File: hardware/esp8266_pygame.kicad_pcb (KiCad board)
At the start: 2 copper layers, 73 parts, among them J1 Conn_02x02_Odd_Even, J2 Conn_01x02, J3 USB_C_Receptacle_USB2.0_16P, J4 Conn_01x07, J5 Conn_01x07, J6 Conn_01x08, Q1 PNP, Q2 NPN, SW1 SW_Push, SW2 SW_Push, SW3 SW_Push, SW4 SW_Push, SW5 SW_Push, SW6 SW_Push, SW7 SW_Push, SW8 SW_Push, U1 ESP-07, U2 SW_SPDT_3pin, U3 HX3242, U4 TP4056, U5 FS8502A, U6 DW01A, U7 AP2112K-3.3, U8 PCF8574T

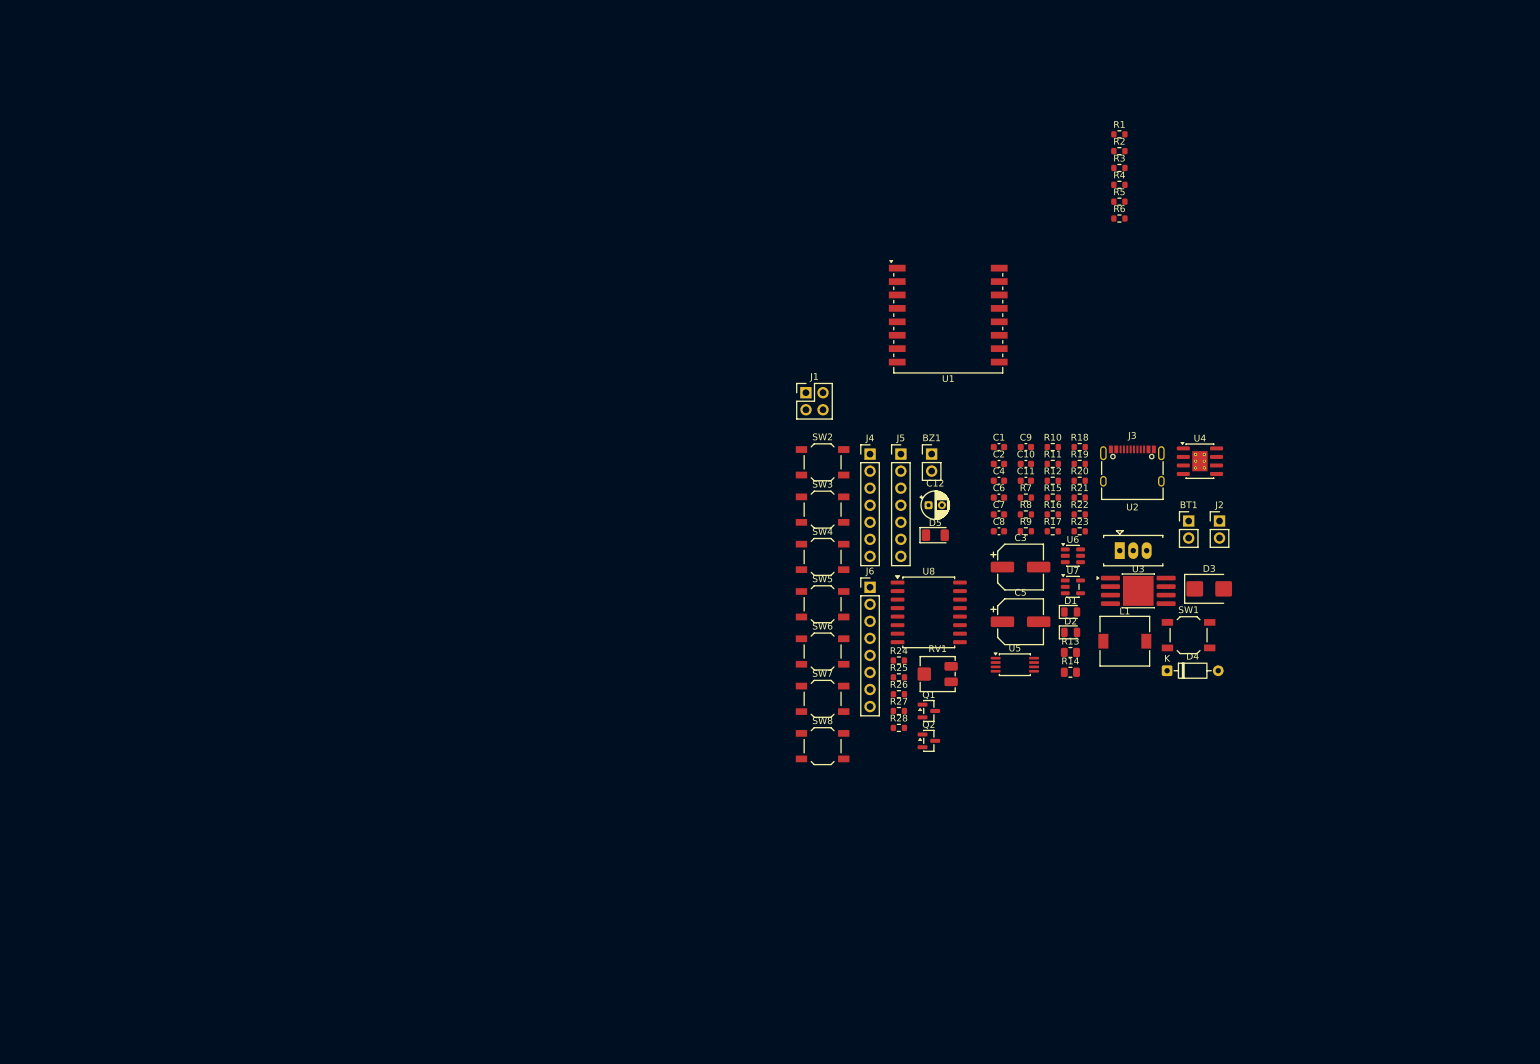
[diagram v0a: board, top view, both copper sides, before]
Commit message: Initial PCB placement and some schematic changes
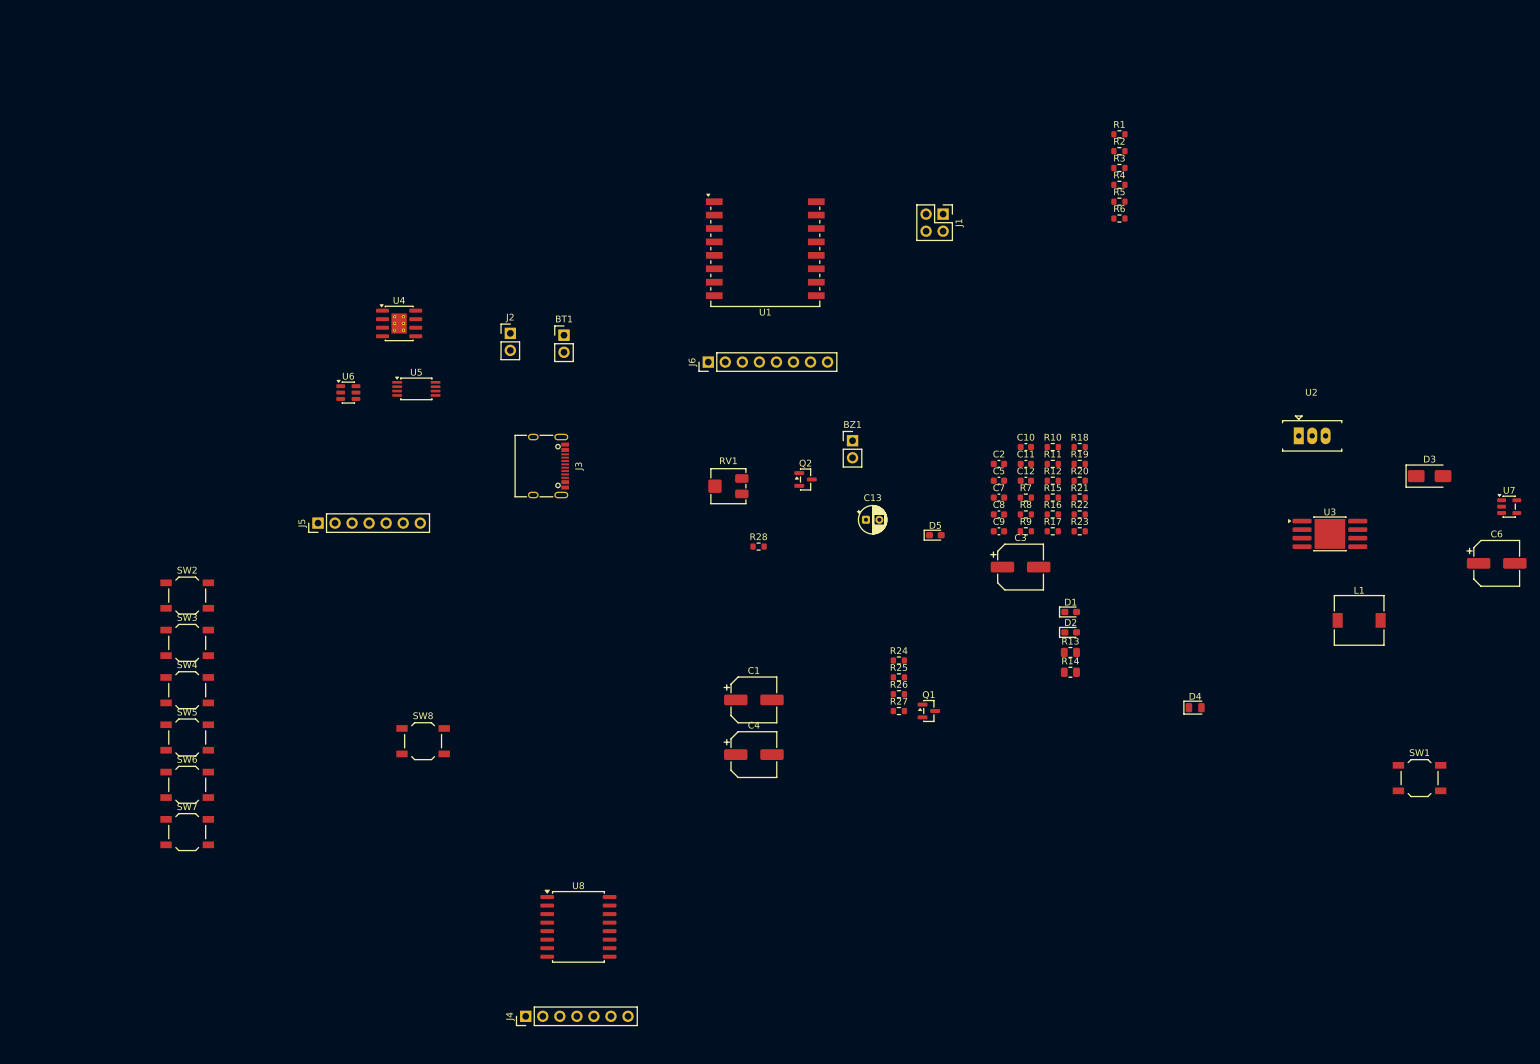
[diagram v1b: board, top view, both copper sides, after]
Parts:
- added C4: 1u, Capacitor_SMD:CP_Elec_6.3x3, F.Cu at (122.8, 148.0)
- C1: value 100n -> 100u; footprint Capacitor_SMD:C_0603_1608Metric -> Capacitor_SMD:CP_Elec_6.3x3
- D1, D2: footprint Diode_SMD:D_0805_2012Metric -> Diode_SMD:D_0603_1608Metric_Pad1.05x0.95mm_HandSolder
- D3: footprint Diode_SMD:D_SMB -> Diode_SMD:D_SMA
- D4: value 1N4148 -> D; footprint Diode_THT:D_DO-35_SOD27_P7.62mm_Horizontal -> Diode_SMD:D_0805_2012Metric
- D5: footprint LED_SMD:LED_1206_3216Metric -> Diode_SMD:D_0603_1608Metric_Pad1.05x0.95mm_HandSolder
- moved U4 121.1 mm to (69.9, 83.8)
- moved U6 110.7 mm to (62.4, 94.0)
- moved J2 109.3 mm to (86.5, 85.2)
- moved J4 98.2 mm to (88.8, 187.0), turned to 90 degrees
- moved U5 98.2 mm to (72.5, 93.5)
- moved BT1 97.1 mm to (94.5, 85.5)
- moved SW6 96.8 mm to (38.4, 152.5)
- moved SW7 96.8 mm to (38.4, 159.6)
- moved SW2 96.8 mm to (38.4, 124.3)
- moved SW3 96.8 mm to (38.4, 131.3)
- moved SW4 96.8 mm to (38.4, 138.4)
- moved SW5 96.8 mm to (38.4, 145.4)
- moved J3 88.2 mm to (91.0, 105.0), turned to -90 degrees
- moved J5 87.5 mm to (57.8, 113.5), turned to 90 degrees
- moved C6 71.5 mm to (233.5, 119.5)
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- renumbered C9 to C10, C10 to C11, C11 to C12, C12 to C13, C4 to C5, C5 to C6, C6 to C7, C7 to C8, C8 to C9
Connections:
- C1 pad 1: GND -> +VSW
- C1 pad 2: +VSW -> GND

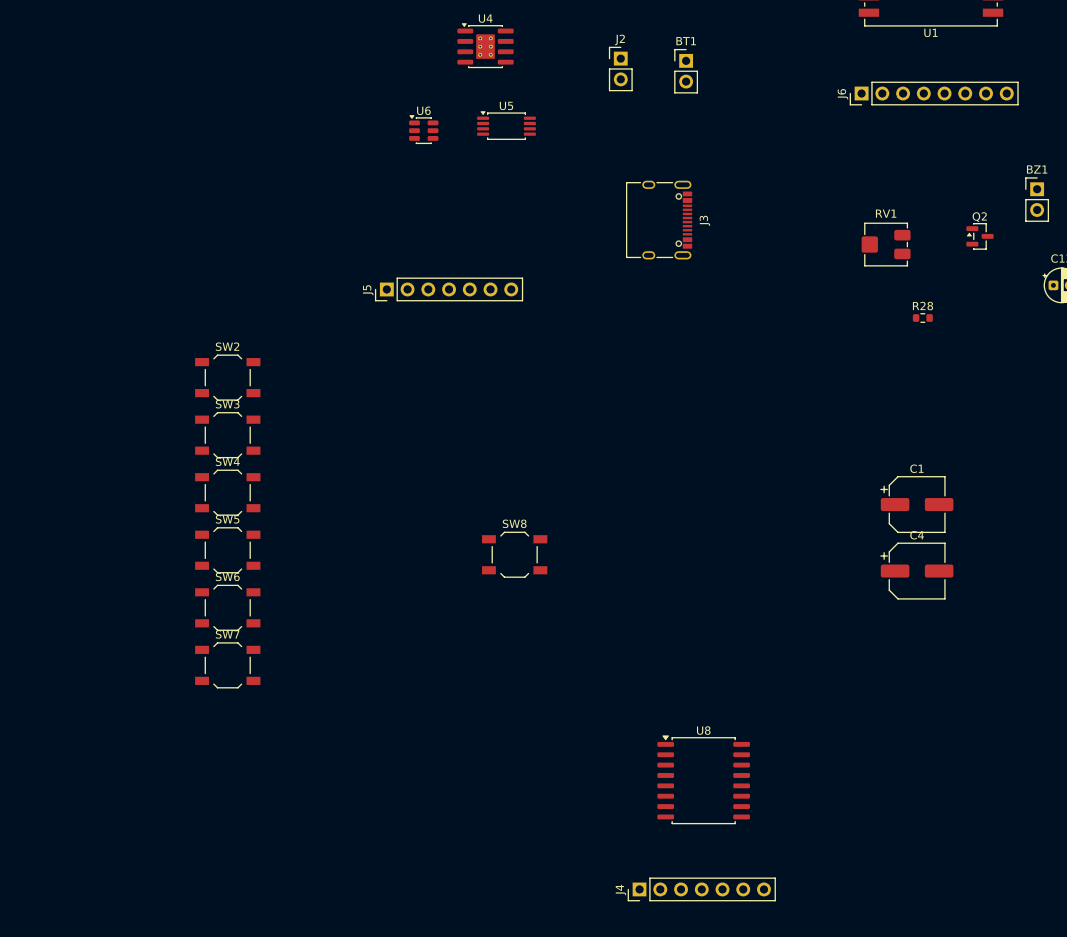
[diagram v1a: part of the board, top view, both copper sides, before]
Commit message: Fixed keypad connector
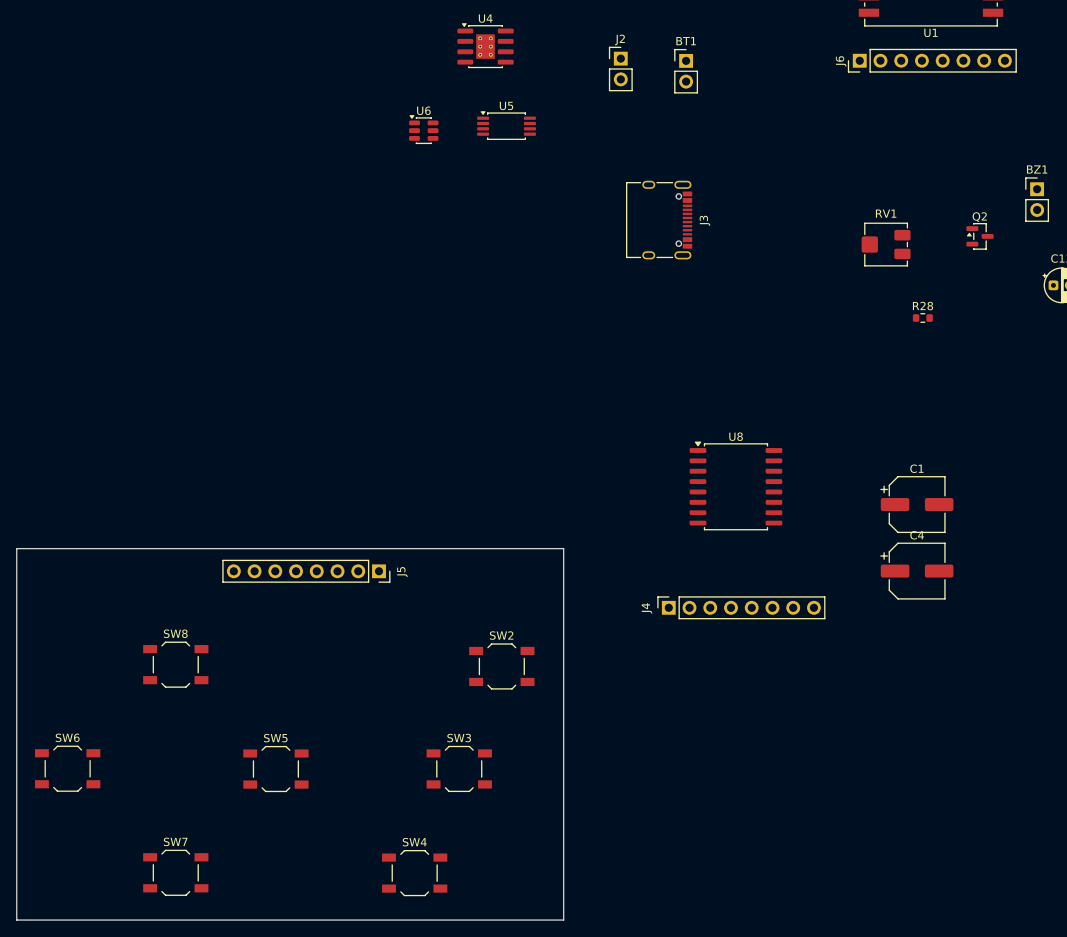
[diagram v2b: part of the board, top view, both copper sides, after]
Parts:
- J4, J5: value Conn_01x07 -> Conn_01x08; footprint Connector_PinHeader_2.54mm:PinHeader_1x07_P2.54mm_Vertical -> Connector_PinSocket_2.54mm:PinSocket_1x08_P2.54mm_Vertical
- moved SW4 51.9 mm to (61.2, 185.0)
- moved SW3 49.8 mm to (66.7, 172.2)
- moved SW2 48.8 mm to (71.9, 159.7)
- moved SW8 43.6 mm to (32.0, 159.5)
- moved U8 36.2 mm to (100.6, 137.7)
- moved J4 34.7 mm to (92.4, 152.5)
- moved J5 34.5 mm to (56.9, 148.0), turned to -90 degrees
- moved SW6 27.8 mm to (18.7, 172.2)
- moved SW5 27.4 mm to (44.2, 172.2)
- moved SW7 26.2 mm to (32.0, 185.0)
- moved J6 4.02 mm to (115.8, 85.5)
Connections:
- SW2 pad 2: GND -> /Human Machine Interface Section/BTN_GND
- SW3 pad 2: GND -> /Human Machine Interface Section/BTN_GND
- SW4 pad 2: GND -> /Human Machine Interface Section/BTN_GND
- SW5 pad 2: GND -> /Human Machine Interface Section/BTN_GND
- SW6 pad 2: GND -> /Human Machine Interface Section/BTN_GND
- SW7 pad 2: GND -> /Human Machine Interface Section/BTN_GND
- SW8 pad 2: GND -> /Human Machine Interface Section/BTN_GND
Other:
- board outline added: 67 x 45.5 mm

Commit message: Audio improvements
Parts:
- removed the C4 at (122.8, 148.0)
- removed Q2: NPN, Package_TO_SOT_SMD:SOT-23
- added C13: 100n, Capacitor_SMD:C_0603_1608Metric, F.Cu at (172.2, 94.6)
- added C14: 10n, Capacitor_SMD:C_0603_1608Metric, F.Cu at (172.2, 97.2)
- added C15: 10u, Capacitor_THT:CP_Radial_D4.0mm_P2.00mm, F.Cu at (176.0, 96.2)
- added C16: 47n, Capacitor_SMD:C_0603_1608Metric, F.Cu at (172.2, 99.7)
- added C17: 220u, Capacitor_THT:CP_Radial_D4.0mm_P2.00mm, F.Cu at (176.0, 101.7)
- added R29: 10k, Resistor_SMD:R_0603_1608Metric, F.Cu at (172.2, 104.7)
- added R30: 10, Resistor_SMD:R_0603_1608Metric, F.Cu at (172.2, 107.2)
- added U9: LM386, Package_SO:SO-8_3.9x4.9mm_P1.27mm, F.Cu at (178.4, 107.8)
- moved R8 137.1 mm to (40.8, 50.7)
- moved R7 135.3 mm to (40.8, 52.5)
- moved D2 131.0 mm to (69.9, 45.2), turned to 90 degrees
- moved C2 129.2 mm to (40.0, 55.2), turned to 90 degrees
- moved D1 127.7 mm to (71.8, 45.2), turned to 90 degrees
- moved R12 117.7 mm to (65.4, 48.2), turned to 180 degrees
- moved R11 115.7 mm to (65.4, 50.0), turned to 180 degrees
- moved R15 108.0 mm to (63.0, 82.0), turned to 90 degrees
- moved R19 105.3 mm to (66.2, 98.5)
- moved R23 102.2 mm to (72.5, 88.8)
- moved C11 101.1 mm to (64.0, 88.2)
- moved J3 79.4 mm to (33.0, 50.7)
- moved C1 77.8 mm to (199.7, 127.8)
- moved R2 69.4 mm to (112.0, 81.8), turned to 90 degrees
- moved R9 69.2 mm to (101.0, 84.8)
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- renumbered C11 to C10, C12 to C11, C13 to C12, C5 to C4, C6 to C5, C7 to C6, C8 to C7, C9 to C8, C10 to C9
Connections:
- BZ1 pad 1: +3.3V -> Net-(BZ1--)
- BZ1 pad 2: Net-(BZ1-+) -> GND
- J4 pad 5: /Human Machine Interface Section/Left_Button_CONN -> GND
- J4 pad 8: GND -> /Human Machine Interface Section/Left_Button_CONN
- J5 pad 5: /Human Machine Interface Section/Left_Button -> /Human Machine Interface Section/BTN_GND
- J5 pad 8: /Human Machine Interface Section/BTN_GND -> /Human Machine Interface Section/Left_Button
- R28 pad 1: Net-(R28-Pad1) -> /BUZZER
- RV1 pad 2: /BUZZER -> Net-(C14-Pad2)
- RV1 pad 3: Net-(R28-Pad1) -> Net-(U9-+)
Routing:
- net /Human Machine Interface Section/Left_Button: track 0.00 -> 39.0 mm
- net /Human Machine Interface Section/Down_Button: track 0.00 -> 38.8 mm
- net /Human Machine Interface Section/C_Button: track 0.00 -> 37.7 mm
- net /Human Machine Interface Section/B_Button: track 0.00 -> 27.0 mm
- net /Human Machine Interface Section/Right_Button: track 0.00 -> 23.1 mm
- net /Human Machine Interface Section/UP_Button_CONN: track 0.00 -> 20.2 mm
- net /Human Machine Interface Section/A_Button_CONN: track 0.00 -> 19.4 mm
- net /Human Machine Interface Section/Down_Button_CONN: track 0.00 -> 19.4 mm
- net /Human Machine Interface Section/A_Button: track 0.00 -> 19.4 mm
- net /Human Machine Interface Section/UP_Button: track 0.00 -> 18.7 mm
- net /Human Machine Interface Section/Left_Button_CONN: track 0.00 -> 18.5 mm
- net /Human Machine Interface Section/B_Button_CONN: track 0.00 -> 17.5 mm
- net /Human Machine Interface Section/C_Button_CONN: track 0.00 -> 16.4 mm
- net /Human Machine Interface Section/Right_Button_CONN: track 0.00 -> 15.5 mm
- net /SCL: track 0.00 -> 11.6 mm
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- added copper zone on F.Cu, net /Human Machine Interface Section/BTN_GND
- added copper zone on F.Cu, net GND
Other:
- board size 67 x 45.5 mm -> 104.7 x 66.1 mm
